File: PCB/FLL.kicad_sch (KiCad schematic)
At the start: 9 parts, among them U1 MCP73831-2-MC, U3 LM317L_SOT-89

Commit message: chore: Remove unnecessary files and update PCB design configuration
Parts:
- added C1: 1uF, symbol Device:C_Small
- added C3: 0,1uF, symbol Device:C_Small
- added C4: 4,5uF, symbol Device:C_Small
- added POT1: 240Ω, symbol Device:R
- added POT2: 1,4kΩ, symbol Device:R
- C2: value C_Small -> 100uF
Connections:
- net at F1.1, U3.2 (VO): now also POT1.1
- net at F1.2: now also U1.1 (V_{DD}), U1.2 (V_{DD}), C1.2
- net -7.5V: now reaches C2.1, D1.2 (A), D3.1 (K), L1.1 (-)
- net -7.5V: now also U1.6 (V_{SS}), C4.2
- net at C2.2, D2.1 (K), D4.2 (A)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: now also C3.2; no longer U3.1 (ADJ)
- net +7.5V: now reaches U1.3 (V_{BAT}), U1.4 (V_{BAT})
- net +7.5V: now also C4.1
- net +1V0: now reaches U1.5 (STAT)
- new net: POT1.2, POT2.2, U3.1 (ADJ)
- new net GND: C1.1, C3.1, POT2.1
- no-connect marks 1 -> 6

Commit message: chore: Remove unnecessary files and update PCB design configuration
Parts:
- removed D1, D2, D3, D4: 1N4007, Diode_THT:D_DO-41_SOD81_P10.16mm_Horizontal, symbol Diode:1N4007
- added POT3: 1kΩ, symbol Device:R
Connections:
- net +16V: now reaches C2.2, C3.2, L1.2 (+), U3.3 (VI)
- net at U1.8 (PROG): now also POT3.1
- net -7.5V renamed -16V
- net -16V: now also POT3.2
- no-connect marks 6 -> 5
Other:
- note added: "Powersupply 16V"
- note removed: "Gleichrichter"

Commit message: chore: Update PCB design configuration and remove unnecessary files
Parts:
- added D1|2,2V1: LED Blau, symbol Device:LED
- added POT4: 240Ω, symbol Device:R
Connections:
- net GND is gone; now on net +16V: C1.1, C3.1, POT2.1
- net +16V: now also POT4.2
- net -16V: now also D1|2,2V1.2 (A)
- net 7,3V |1A Output: now reaches C1.2, F1.2, U1.1 (V_{DD}), U1.2 (V_{DD})
- new net: D1|2,2V1.1 (K), POT4.1
- no-connect marks 5 -> 6
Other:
- note added: "Batterieladeregler"
- note added: "Flattening"
- note added: "Powersupply 16V AC"
- note removed: "Powersupply 16V"
- moved on the sheet: C1, C2, C3, C4, F1, L1, POT1, POT2, POT3, U1, U3

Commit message: chore: Update PCB design configuration and remove unnecessary files
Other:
- note removed: "04.07.2024"
- note removed: "First Layer"
- company: (none) -> https://github.com/Ekips-Prime-Pro
- title: (none) -> LargeHubBattery Charger LEGO: 45610
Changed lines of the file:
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@@
 	(generator_version "8.0")
 	(paper "A4")
+	(title_block
+		(title "LargeHubBattery Charger LEGO: 45610")
+		(date "04.07.2024")
+		(company "https://github.com/Ekips-Prime-Pro")
+		(comment 1 "1. Powersupply, 2. Flattening, 3. Spanungsregler, 4.Batterieladeregler")
+	)
 	(junction
 		(at 152.4 83.82)
@@
 		(fill
 			(type none)
-		)
-	)
-	(text "04.07.2024"
-		(exclude_from_sim no)
-		(at 211.836 193.548 0)
-		(effects
-			(font
-				(size 1.27 1.27)
-			)
 		)
 	)
@@
 		(effects
 			(font
-				(size 1.27 1.27)
-			)
-		)
-	)
-	(text "First Layer"
-		(exclude_from_sim no)
-		(at 191.77 189.738 0)
-		(effects
-			(font

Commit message: chore: Update PCB design configuration and remove unnecessary files
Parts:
- C1, C4: footprint (none) -> Capacitor_THT:CP_Axial_L10.0mm_D4.5mm_P15.00mm_Horizontal
- C2: footprint (none) -> Capacitor_THT:CP_Axial_L11.0mm_D6.0mm_P18.00mm_Horizontal
- C3: value 0,1uF -> 0,47uF; footprint (none) -> Capacitor_SMD:C_Elec_6.3x5.4
- D1|2,2V1: footprint (none) -> LED_THT:LED_D3.0mm_Horizontal_O6.35mm_Z10.0mm
- F1: footprint (none) -> Fuse:Fuse_Bourns_MF-RG300
- L1: footprint (none) -> Inductor_SMD:L_Neosid_Air-Coil_SML_6turn_HAM0631A
- POT1, POT2, POT3, POT4: footprint (none) -> Resistor_SMD:R_0603_1608Metric_Pad0.98x0.95mm_HandSolder
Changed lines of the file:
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@@
 			)
 		)
-		(property "Footprint" ""
+		(property "Footprint" "Fuse:Fuse_Bourns_MF-RG300"
 			(at 152.4 82.55 0)
 			(effects
@@
 			)
 		)
-		(property "Value" "0,1uF"
+		(property "Value" "0,47uF"
 			(at 119.3863 74.93 90)
 			(effects
@@
 			)
 		)
-		(property "Footprint" ""
+		(property "Footprint" "Capacitor_SMD:C_Elec_6.3x5.4"
 			(at 119.38 78.74 0)
 			(effects
@@
 			)
 		)
-		(property "Footprint" ""
+		(property "Footprint" "Inductor_SMD:L_Neosid_Air-Coil_SML_6turn_HAM0631A"
 			(at 78.105 125.73 90)
 			(effects
@@
 			)
 		)
-		(property "Footprint" ""
+		(property "Footprint" "Resistor_SMD:R_0603_1608Metric_Pad0.98x0.95mm_HandSolder"
 			(at 140.462 90.17 90)
 			(effects
@@
 			)
 		)
-		(property "Footprint" ""
+		(property "Footprint" "LED_THT:LED_D3.0mm_Horizontal_O6.35mm_Z10.0mm"
 			(at 66.04 110.49 0)
 			(effects
@@
 			)
 		)
-		(property "Footprint" ""
+		(property "Footprint" "Resistor_SMD:R_0603_1608Metric_Pad0.98x0.95mm_HandSolder"
 			(at 167.132 144.78 90)
 			(effects
@@
 			)
 		)
-		(property "Footprint" ""
+		(property "Footprint" "Capacitor_THT:CP_Axial_L10.0mm_D4.5mm_P15.00mm_Horizontal"
 			(at 209.55 140.97 0)
 			(effects
@@
 			)
 		)
-		(property "Footprint" ""
+		(property "Footprint" "Capacitor_THT:CP_Axial_L10.0mm_D4.5mm_P15.00mm_Horizontal"
 			(at 143.51 76.2 0)
 			(effects
@@
 			)
 		)
-		(property "Footprint" ""
+		(property "Footprint" "Capacitor_THT:CP_Axial_L11.0mm_D6.0mm_P18.00mm_Horizontal"
 			(at 86.36 109.22 0)
 			(effects
@@
 			)
 		)
-		(property "Footprint" ""
+		(property "Footprint" "Resistor_SMD:R_0603_1608Metric_Pad0.98x0.95mm_HandSolder"
 			(at 64.262 125.73 90)
 			(effects
@@
 			)
 		)
-		(property "Footprint" ""
+		(property "Footprint" "Resistor_SMD:R_0603_1608Metric_Pad0.98x0.95mm_HandSolder"
 			(at 127 99.568 90)
 			(effects

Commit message: chore: Update PCB design configuration and remove unnecessary files
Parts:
- removed C2: 100uF, Capacitor_THT:CP_Axial_L11.0mm_D6.0mm_P18.00mm_Horizontal, symbol Device:C_Small
- removed D1|2,2V1: LED Blau, LED_THT:LED_D3.0mm_Horizontal_O6.35mm_Z10.0mm, symbol Device:LED
- removed L1: ElectromagneticActor, Inductor_SMD:L_Neosid_Air-Coil_SML_6turn_HAM0631A, symbol Device:ElectromagneticActor
- removed POT4: 240Ω, Resistor_SMD:R_0603_1608Metric_Pad0.98x0.95mm_HandSolder, symbol Device:R
- C3: footprint Capacitor_SMD:C_Elec_6.3x5.4 -> Capacitor_THT:CP_Axial_L10.0mm_D4.5mm_P15.00mm_Horizontal
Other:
- note removed: "Flattening"

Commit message: chore: Update PCB design configuration and remove unnecessary files
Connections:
- net +16V: no longer C1.1, C3.1, POT2.1
- net 7,3V |1A Output: no longer names the net of C1.2, F1.2, U1.1 (V_{DD}), U1.2 (V_{DD})
- new net GND: C1.1, C3.1, POT2.1
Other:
- moved on the sheet: C3
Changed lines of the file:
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@@
 		(date "04.07.2024")
 		(company "https://github.com/Ekips-Prime-Pro")
-		(comment 1 "1. Powersupply, 2. Flattening, 3. Spanungsregler, 4.Batterieladeregler")
+		(comment 1 "1. Powersupply, 2. Spanungsregler, 3.Batterieladeregler")
 	)
 	(junction
@@
 	)
 	(junction
-		(at 123.19 83.82)
-		(diameter 0)
-		(color 0 0 0 0)
-	)
-	(junction
 		(at 132.08 93.98)
 		(diameter 0)
@@
 	)
 	(junction
-		(at 115.57 78.74)
-		(diameter 0)
-		(color 0 0 0 0)
-	)
-	(junction
 		(at 115.57 97.79)
 		(diameter 0)
@@
 	)
 	(junction
-		(at 121.92 97.79)
+		(at 121.92 83.82)
 		(diameter 0)
 		(color 0 0 0 0)
@@
 	(junction
 		(at 168.91 153.67)
+		(diameter 0)
+		(color 0 0 0 0)
+	)
+	(junction
+		(at 115.57 83.82)
 		(diameter 0)
 		(color 0 0 0 0)
@@
 	)
 	(no_connect
+		(at 121.92 97.79)
+	)
+	(no_connect
 		(at 189.23 143.51)
 	)
@@
 		(at 179.07 118.11)
 	)
-	(no_connect
-		(at 115.57 93.98)
-	)
 	(wire
 		(pts
@@
 	(wire
 		(pts
-			(xy 121.92 97.79) (xy 123.19 97.79)
-		)
-		(stroke
-			(width 0)
-			(type default)
-		)
-	)
-	(wire
-		(pts
 			(xy 209.55 133.35) (xy 205.74 133.35)
 		)
@@
 	(wire
 		(pts
-			(xy 121.92 129.54) (xy 121.92 97.79)
+			(xy 121.92 83.82) (xy 121.92 129.54)
 		)
 		(stroke
@@
 	(wire
 		(pts
-			(xy 121.92 83.82) (xy 123.19 83.82)
-		)
-		(stroke
-			(width 0)
-			(type default)
-		)
-	)
-	(wire
-		(pts
-			(xy 115.57 78.74) (xy 115.57 76.2)
+			(xy 121.92 83.82) (xy 124.46 83.82)
+		)
+		(stroke
+			(width 0)
+			(type default)
+		)
+	)
+	(wire
+		(pts
+			(xy 115.57 76.2) (xy 115.57 83.82)
 		)
 		(stroke
@@
 		(stroke
 			(width 0)
-			(type default)
+			(type solid)
 		)
 	)
@@
 	(wire
 		(pts
-			(xy 121.92 97.79) (xy 115.57 97.79)
+			(xy 115.57 97.79) (xy 123.19 97.79)
 		)
 		(stroke
@@
 	(wire
 		(pts
-			(xy 123.19 78.74) (xy 123.19 83.82)
-		)
-		(stroke
-			(width 0)
-			(type default)
-		)
-	)
-	(wire
-		(pts
 			(xy 189.23 138.43) (xy 189.23 153.67)
 		)
@@
 	(wire
 		(pts
-			(xy 121.92 78.74) (xy 123.19 78.74)
-		)
-		(stroke
-			(width 0)
-			(type default)
-		)
-	)
-	(wire
-		(pts
 			(xy 199.39 118.11) (xy 199.39 143.51)
 		)
@@
 	(wire
 		(pts
-			(xy 121.92 97.79) (xy 121.92 83.82)
-		)
-		(stroke
-			(width 0)
-			(type default)
-		)
-	)
-	(wire
-		(pts
 			(xy 152.4 83.82) (xy 152.4 76.2)
 		)
@@
 	(wire
 		(pts
-			(xy 123.19 83.82) (xy 124.46 83.82)
-		)
-		(stroke
-			(width 0)
-			(type default)
-		)
-	)
-	(wire
-		(pts
 			(xy 146.05 76.2) (xy 152.4 76.2)
 		)
@@
 	(wire
 		(pts
-			(xy 116.84 78.74) (xy 115.57 78.74)
-		)
-		(stroke
-			(width 0)
-			(type default)
-		)
-	)
-	(wire
-		(pts
-			(xy 115.57 97.79) (xy 115.57 78.74)
+			(xy 116.84 83.82) (xy 115.57 83.82)
+		)
+		(stroke
+			(width 0)
+			(type default)
+		)
+	)
+	(wire
+		(pts
+			(xy 115.57 97.79) (xy 115.57 83.82)
 		)
 		(stroke
@@
 				(size 1.27 1.27)
 			)
-		)
-	)
-	(label "GND for batterie"
-		(at 138.43 118.11 0)
-		(fields_autoplaced yes)
-		(effects
-			(font
-				(size 1.27 1.27)
-			)
-			(justify left bottom)
-		)
-	)
-	(label "-16V | -1A"
-		(at 129.54 153.67 0)
-		(fields_autoplaced yes)
-		(effects
-			(font
-				(size 1.27 1.27)
-			)
-			(justify left bottom)
-		)
-	)
-	(label "16V | 1A"
-		(at 111.76 129.54 0)
-		(fields_autoplaced yes)
-		(effects
-			(font
-				(size 1.27 1.27)
-			)
-			(justify left bottom)
-		)
-	)
-	(label "7,3V |1A Output"
-		(at 161.29 83.82 0)
-		(fields_autoplaced yes)
-		(effects
-			(font
-				(size 1.27 1.27)
-			)
-			(justify left bottom)
 		)
 	)
@@
 	(symbol
 		(lib_id "Device:C_Small")
-		(at 119.38 78.74 90)
+		(at 119.38 83.82 90)
 		(unit 1)
 		(exclude_from_sim no)
@@
 		(fields_autoplaced yes)
 		(property "Reference" "C3"
-			(at 119.3863 72.39 90)
+			(at 119.3863 77.47 90)
 			(effects
 				(font
@@
 		)
 		(property "Value" "0,47uF"
-			(at 119.3863 74.93 90)
+			(at 119.3863 80.01 90)
 			(effects
 				(font
@@
 		)
 		(property "Footprint" "Capacitor_THT:CP_Axial_L10.0mm_D4.5mm_P15.00mm_Horizontal"
-			(at 119.38 78.74 0)
+			(at 119.38 83.82 0)
 			(effects
 				(font
@@
 		)
 		(property "Datasheet" "~"
-			(at 119.38 78.74 0)
+			(at 119.38 83.82 0)
 			(effects
 				(font
@@
 		)
 		(property "Description" "Unpolarized capacitor, small symbol"
-			(at 119.38 78.74 0)
-			(effects
-				(font
+			(at 119.38 83.82 0)
+			(effects
+				(font

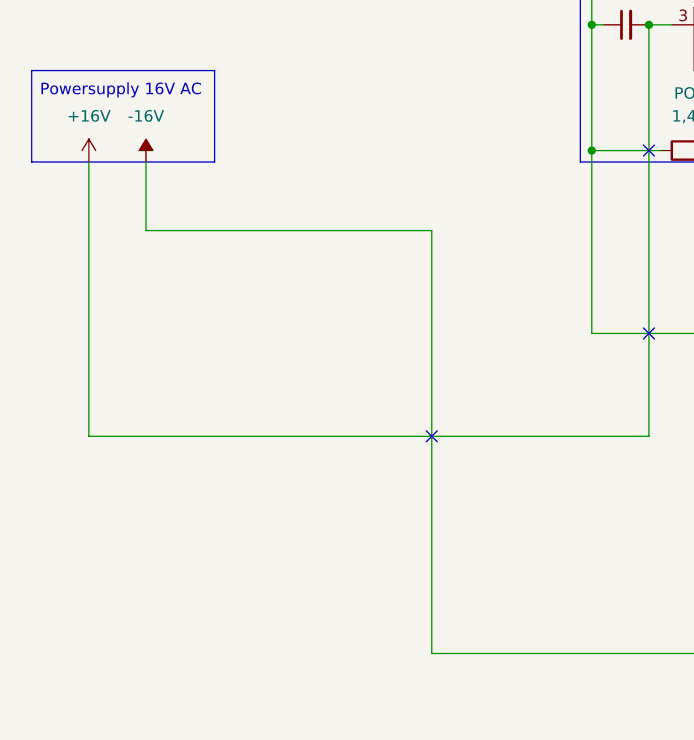
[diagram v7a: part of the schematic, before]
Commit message: Update PCB design configuration and net colors
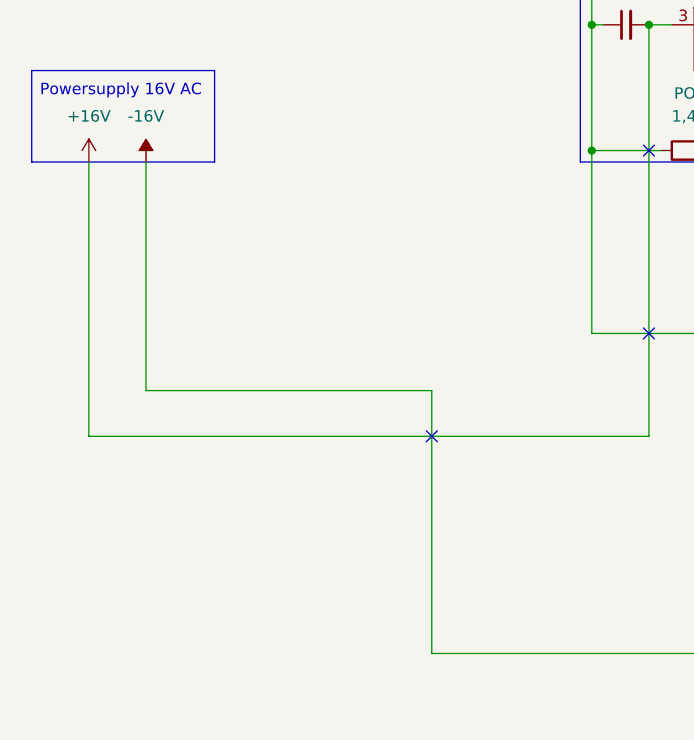
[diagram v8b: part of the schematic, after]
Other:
- title: LargeHubBattery Charger LEGO: 45610 -> Large Hub Battery LEGO: 45610 | Charger
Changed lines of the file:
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@@
 	(paper "A4")
 	(title_block
-		(title "LargeHubBattery Charger LEGO: 45610")
+		(title "Large Hub Battery LEGO: 45610 | Charger")
 		(date "04.07.2024")
 		(company "https://github.com/Ekips-Prime-Pro")
@@
 	(wire
 		(pts
-			(xy 97.79 106.68) (xy 97.79 153.67)
+			(xy 97.79 124.46) (xy 97.79 153.67)
 		)
 		(stroke
@@
 	(wire
 		(pts
-			(xy 66.04 106.68) (xy 97.79 106.68)
+			(xy 66.04 124.46) (xy 97.79 124.46)
 		)
 		(stroke
@@
 	(wire
 		(pts
-			(xy 66.04 99.06) (xy 66.04 106.68)
-		)
-		(stroke
+			(xy 66.04 99.06) (xy 66.04 124.46)
+		)
+		(stroke
